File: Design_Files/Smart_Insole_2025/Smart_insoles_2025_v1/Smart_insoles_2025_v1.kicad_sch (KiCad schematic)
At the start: 14 parts, among them IC1 USBLC6-2SC6, J2 USB_C_Receptacle_USB2.0_16P, SW1 RESET, SW2 BOOT, U6 ESP32-C3-MINI-1-N4

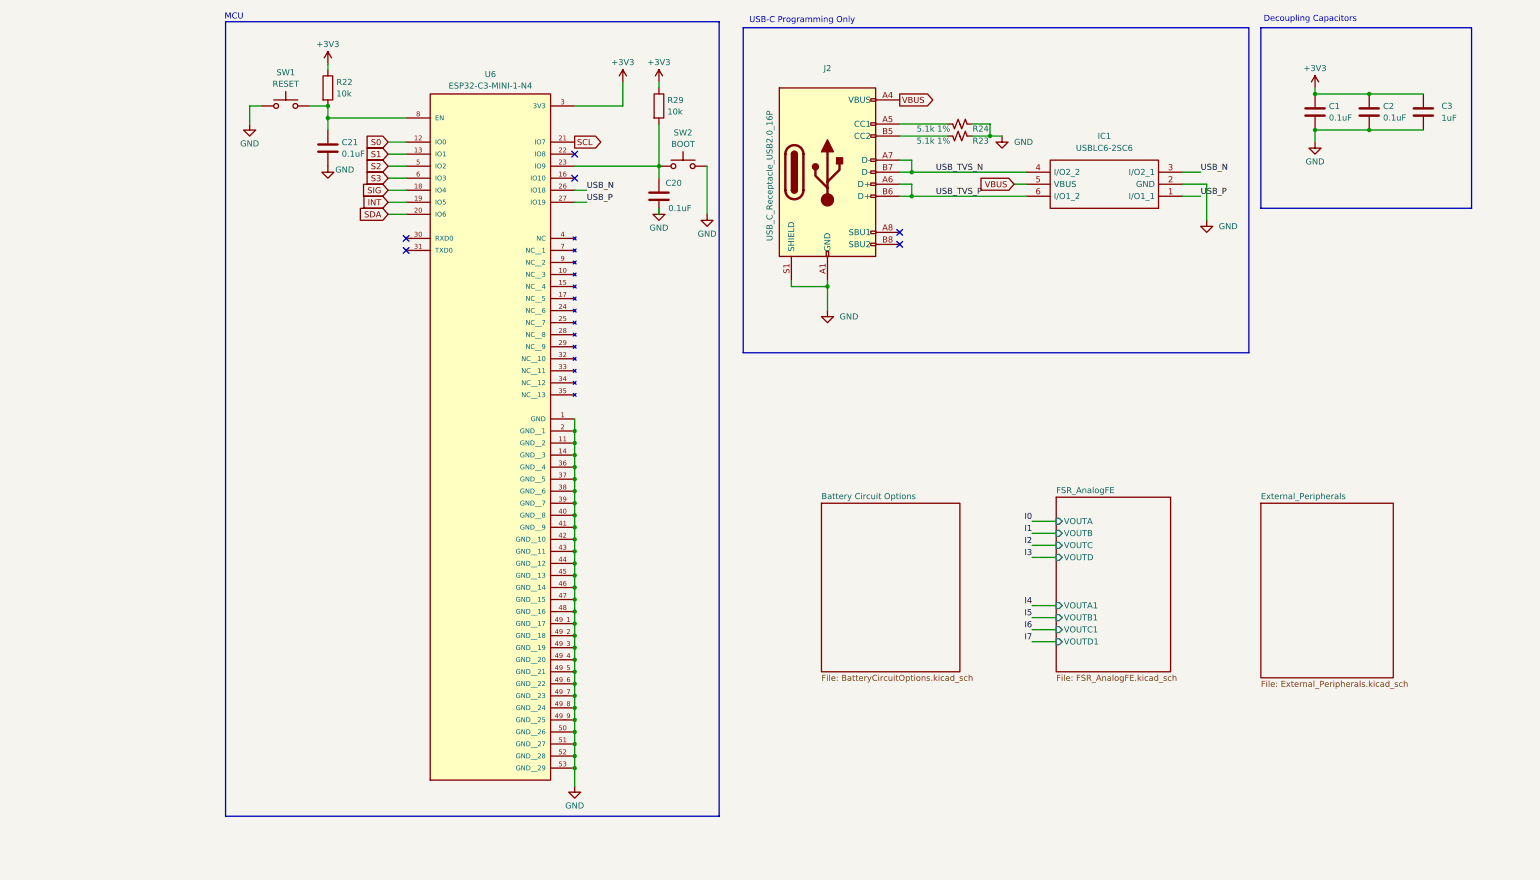
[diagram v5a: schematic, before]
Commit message: SCH: Fixed Warnings. Added thermistor solder pads library.
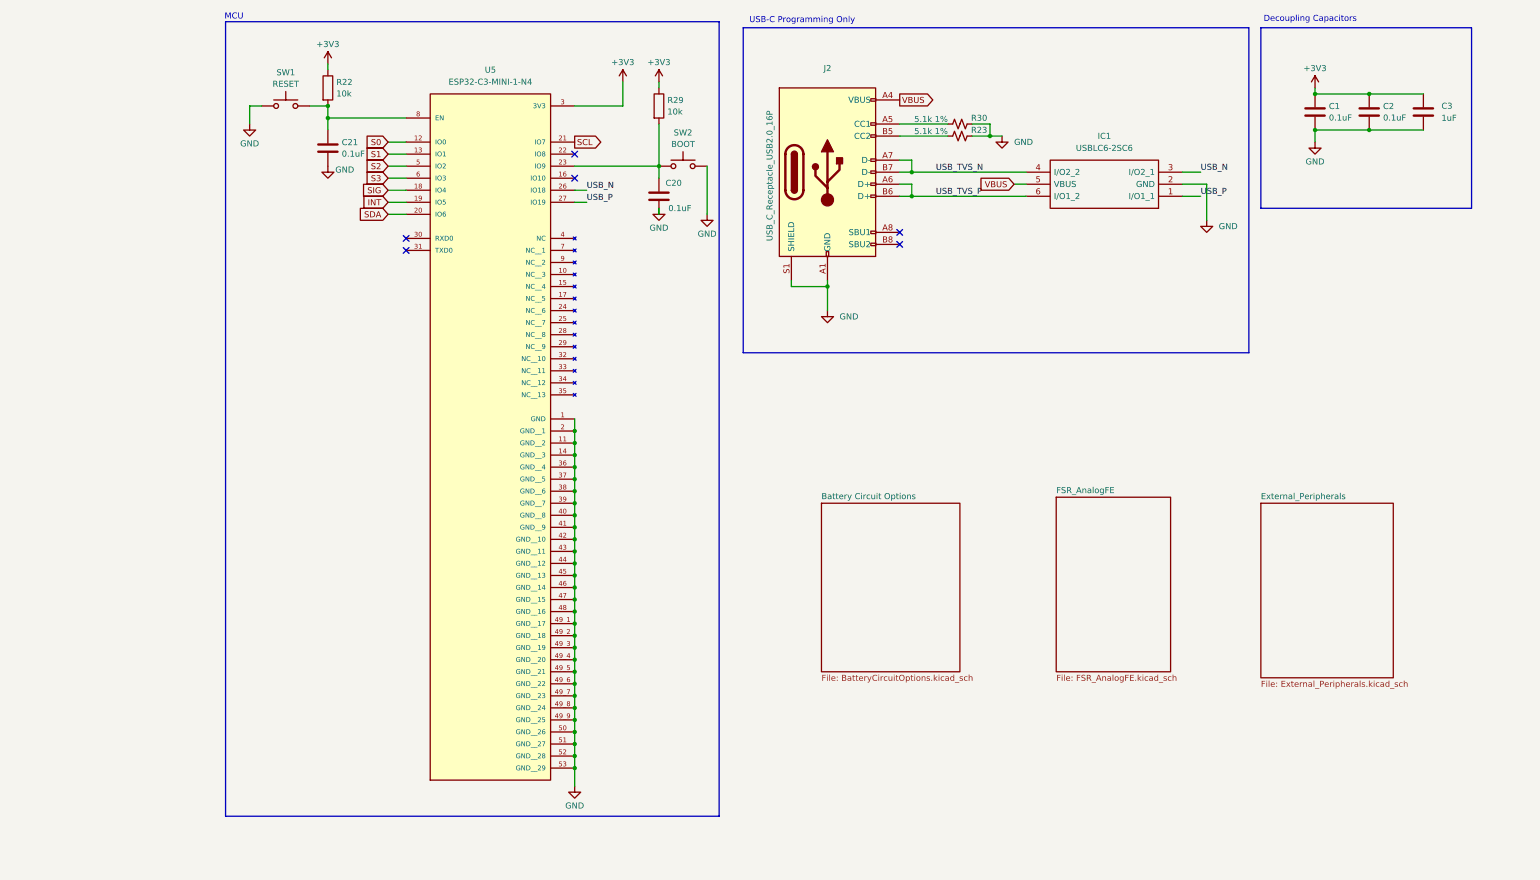
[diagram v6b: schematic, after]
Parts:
- removed R23, R24: 5.1k 1%, Capacitor_SMD:C_0805_2012Metric_Pad1.18x1.45mm_HandSolder, symbol BatteryProtectionCircuit:R_5.1k_Ohm_1%
- removed U6: ESP32-C3-MINI-1-N4, ESP32-C3-MINI-1-N4:XCVR_ESP32-C3-MINI-1-N4, symbol ESP32-C3-MINI-1-N4:ESP32-C3-MINI-1-N4
- added R23, R30: 5.1k 1%, Resistor_SMD:R_0805_2012Metric, symbol Device:R_Small_US
- added U5: ESP32-C3-MINI-1-N4, ESP32-C3-MINI-1-N4:XCVR_ESP32-C3-MINI-1-N4, symbol ESP32-C3-MINI-1-N4:ESP32-C3-MINI-1-N4
- R22, R29: footprint Resistor_SMD:R_0603_1608Metric -> Resistor_SMD:R_0805_2012Metric
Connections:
- net +3V3: now also U5.3 (3V3)
- net GND: now also R23.2, R30.2, U5.1 (GND), U5.11 (GND__2), U5.14 (GND__3), U5.2 (GND__1), U5.36 (GND__4), U5.37 (GND__5), U5.38 (GND__6), U5.39 (GND__7), U5.40 (GND__8), U5.41 (GND__9), U5.42 (GND__10), U5.43 (GND__11), U5.44 (GND__12), U5.45 (GND__13), U5.46 (GND__14), U5.47 (GND__15), U5.48 (GND__16), U5.49_1 (GND__17), U5.49_2 (GND__18), U5.49_3 (GND__19), U5.49_4 (GND__20), U5.49_5 (GND__21), U5.49_6 (GND__22), U5.49_7 (GND__23), U5.49_8 (GND__24), U5.49_9 (GND__25), U5.50 (GND__26), U5.51 (GND__27), U5.52 (GND__28), U5.53 (GND__29)
- net INT: now also U5.19 (IO5)
- net S0: now also U5.12 (IO0)
- net S1: now also U5.13 (IO1)
- net S2: now also U5.5 (IO2)
- net S3: now also U5.6 (IO3)
- net SCL: now also U5.21 (IO7)
- net SDA: now also U5.20 (IO6)
- net SIG: now also U5.18 (IO4)
- net USB_N: now also U5.26 (IO18)
- net USB_P: now also U5.27 (IO19)
- net at C20.2, R29.2, SW2.2: now also U5.23 (IO9)
- net at C21.2, R22.2, SW1.2: now also U5.8 (EN)
- net at J2.B5 (CC2): now also R23.1
- net at J2.A5 (CC1): now also R30.1
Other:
- sheet FSR_AnalogFE ports: added none; removed VOUTA, VOUTA1, VOUTB, VOUTB1, VOUTC, VOUTC1, VOUTD, VOUTD1

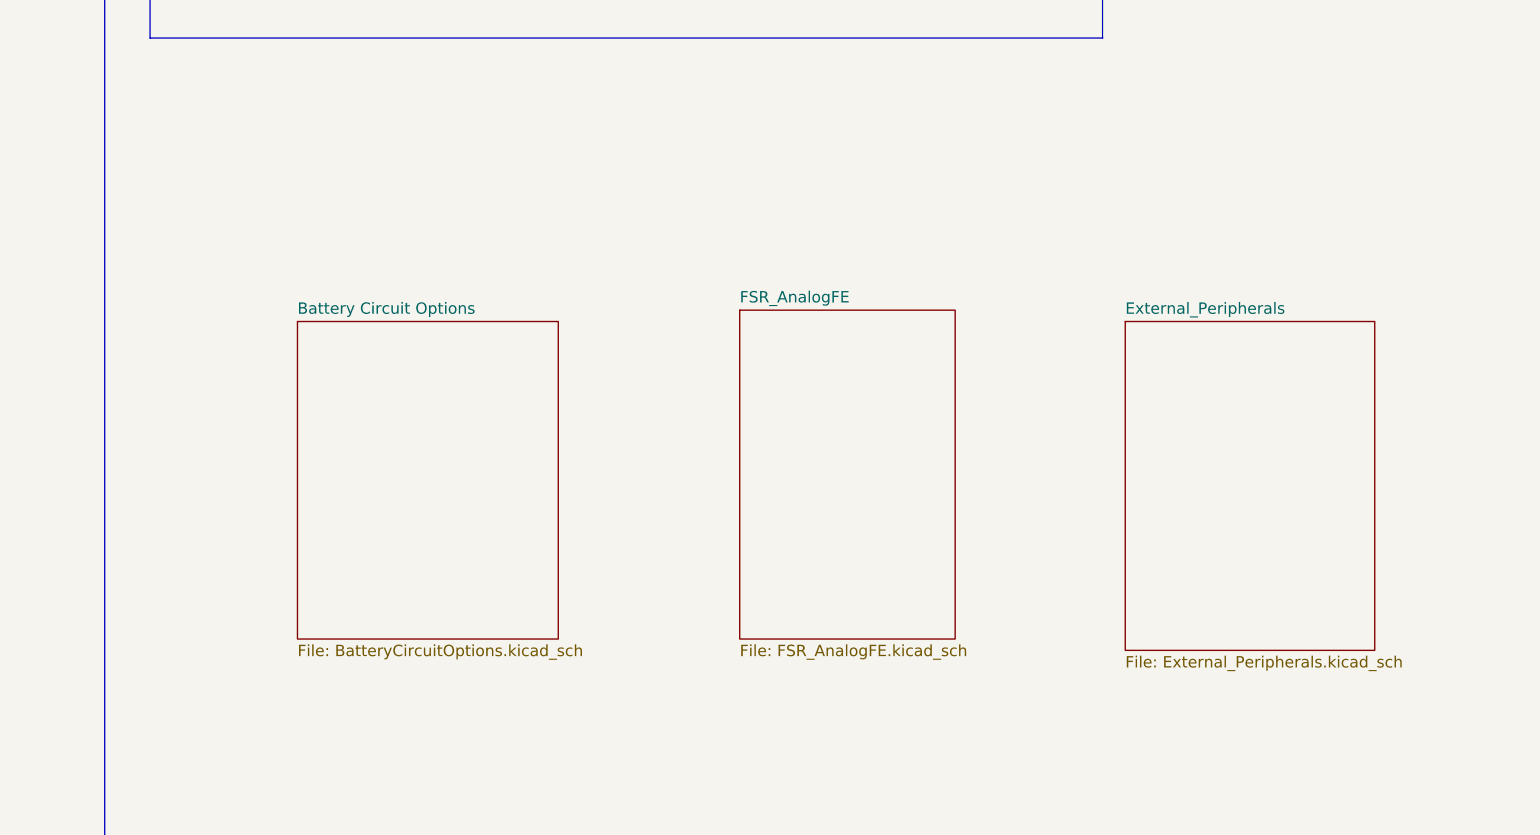
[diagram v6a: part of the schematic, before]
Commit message: SCH: Added Power Test points and Mounting Holes. PCB: Arranged grouped  Footprints to minimize rounting
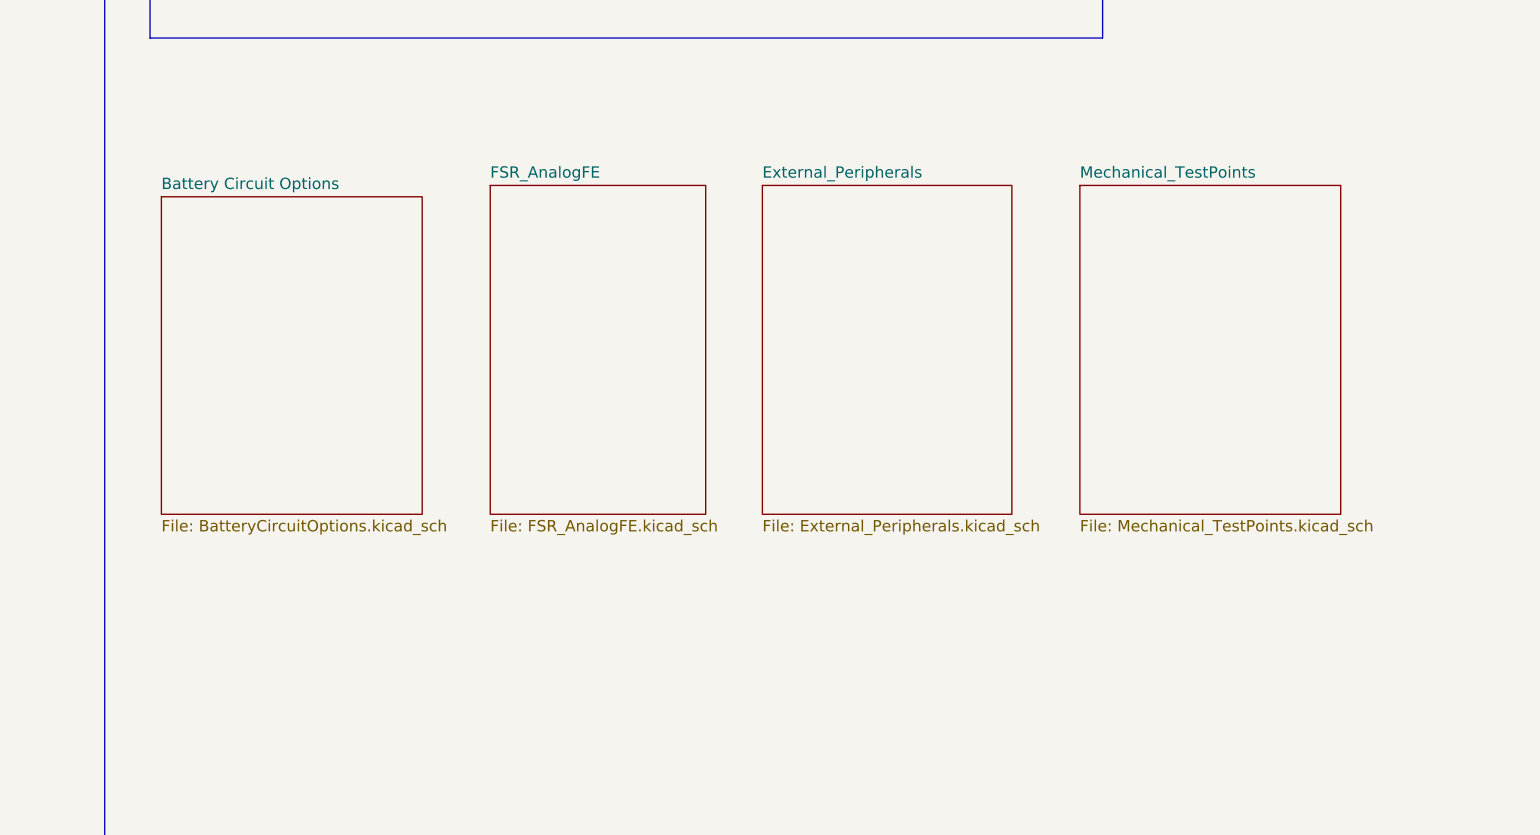
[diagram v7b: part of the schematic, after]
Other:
- added sheet Mechanical_TestPoints (Mechanical_TestPoints.kicad_sch)
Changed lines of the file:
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@@
 	)
 	(sheet
-		(at 234.95 118.11)
+		(at 194.31 102.87)
 		(size 27.94 36.83)
 		(exclude_from_sim no)
@@
 		)
 		(property "Sheetname" "External_Peripherals"
-			(at 234.95 117.3984 0)
+			(at 194.31 102.1584 0)
 			(effects
 				(font
@@
 		)
 		(property "Sheetfile" "External_Peripherals.kicad_sch"
-			(at 234.95 155.5246 0)
+			(at 194.31 140.2846 0)
 			(effects
 				(font
@@
 	)
 	(sheet
-		(at 142.24 118.11)
+		(at 127 104.14)
 		(size 29.21 35.56)
 		(exclude_from_sim no)
@@
 		)
 		(property "Sheetname" "Battery Circuit Options"
-			(at 142.24 117.3984 0)
+			(at 127 103.4284 0)
 			(effects
 				(font
@@
 		)
 		(property "Sheetfile" "BatteryCircuitOptions.kicad_sch"
-			(at 142.24 154.2546 0)
+			(at 127 140.2846 0)
 			(effects
 				(font
@@
 	)
 	(sheet
-		(at 191.77 116.84)
+		(at 229.87 102.87)
+		(size 29.21 36.83)
+		(exclude_from_sim no)
+		(in_bom yes)
+		(on_board yes)
+		(dnp no)
+		(fields_autoplaced yes)
+		(stroke
+			(width 0.1524)
+			(type solid)
+		)
+		(fill
+			(color 0 0 0 0.0000)
+		)
+		(property "Sheetname" "Mechanical_TestPoints"
+			(at 229.87 102.1584 0)
+			(effects
+				(font
+					(size 1.27 1.27)
+				)
+				(justify left bottom)
+			)
+		)
+		(property "Sheetfile" "Mechanical_TestPoints.kicad_sch"
+			(at 229.87 140.2846 0)
+			(effects
+				(font
+					(size 1.27 1.27)
+				)
+				(justify left top)
+			)
+		)
+		(instances
+			(project "Smart_insoles_2025_v1"
+				(path "/f1f3d712-154d-4111-a7c4-f47541abccf8"
+					(page "5")
+				)
+			)
+		)
+	)
+	(sheet
+		(at 163.83 102.87)
 		(size 24.13 36.83)
 		(exclude_from_sim no)
@@
 		)
 		(property "Sheetname" "FSR_AnalogFE"
-			(at 191.77 116.1284 0)
+			(at 163.83 102.1584 0)
 			(effects
 				(font
@@
 		)
 		(property "Sheetfile" "FSR_AnalogFE.kicad_sch"
-			(at 191.77 154.2546 0)
+			(at 163.83 140.2846 0)
 			(effects
 				(font
